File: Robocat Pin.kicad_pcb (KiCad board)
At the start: 2 copper layers, 17 parts, among them SW1 SW_DP3T, U1 NA555P

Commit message: Made PCB, should be good to go now
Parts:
- added G***: LOGO, LOGO, F.Cu at (53.0, 70.6)
- added G***: LOGO, LOGO, F.Cu at (52.9, 52.5)
- added G***: LOGO, LOGO, F.Cu at (52.8, 46.6)
- BT1, C1, C2, C3, C4, C5, C6, R1, R2, R3, R4, R5, R6, SW1: moved to B.Cu
- D1, D2: footprint LED_SMD:LED_1206_3216Metric -> Custom Library:1.3x3.2mm LED; moved to B.Cu
- U1: footprint Package_DIP:DIP-8_W7.62mm -> Custom Library:LM555CM; moved to B.Cu
- moved C4 133.8 mm to (31.8, 48.9), turned to 180 degrees
- moved SW1 128.0 mm to (35.6, 73.0), turned to 135 degrees
- moved D1 126.0 mm to (47.6, 47.6), turned to 180 degrees
- moved U1 105.2 mm to (52.7, 26.0), turned to 180 degrees
- moved C2 103.5 mm to (51.4, 69.8), turned to 180 degrees
- moved C5 101.4 mm to (31.1, 57.1), turned to 180 degrees
- moved D2 100.0 mm to (57.8, 47.6), turned to 180 degrees
- moved R4 99.3 mm to (45.1, 78.7), turned to 180 degrees
- moved BT1 85.2 mm to (52.7, 52.7), turned to 180 degrees
- moved C6 82.8 mm to (74.9, 54.0), turned to 180 degrees
- moved R5 79.8 mm to (47.6, 78.7), turned to 180 degrees
- moved R6 79.7 mm to (50.2, 78.7), turned to 180 degrees
- moved R1 76.5 mm to (55.9, 78.7), turned to 180 degrees
- moved R2 76.1 mm to (58.7, 78.7), turned to 180 degrees
- moved R3 76.0 mm to (61.2, 78.7), turned to 180 degrees
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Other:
- board outline added: 62.9 x 62.9 mm

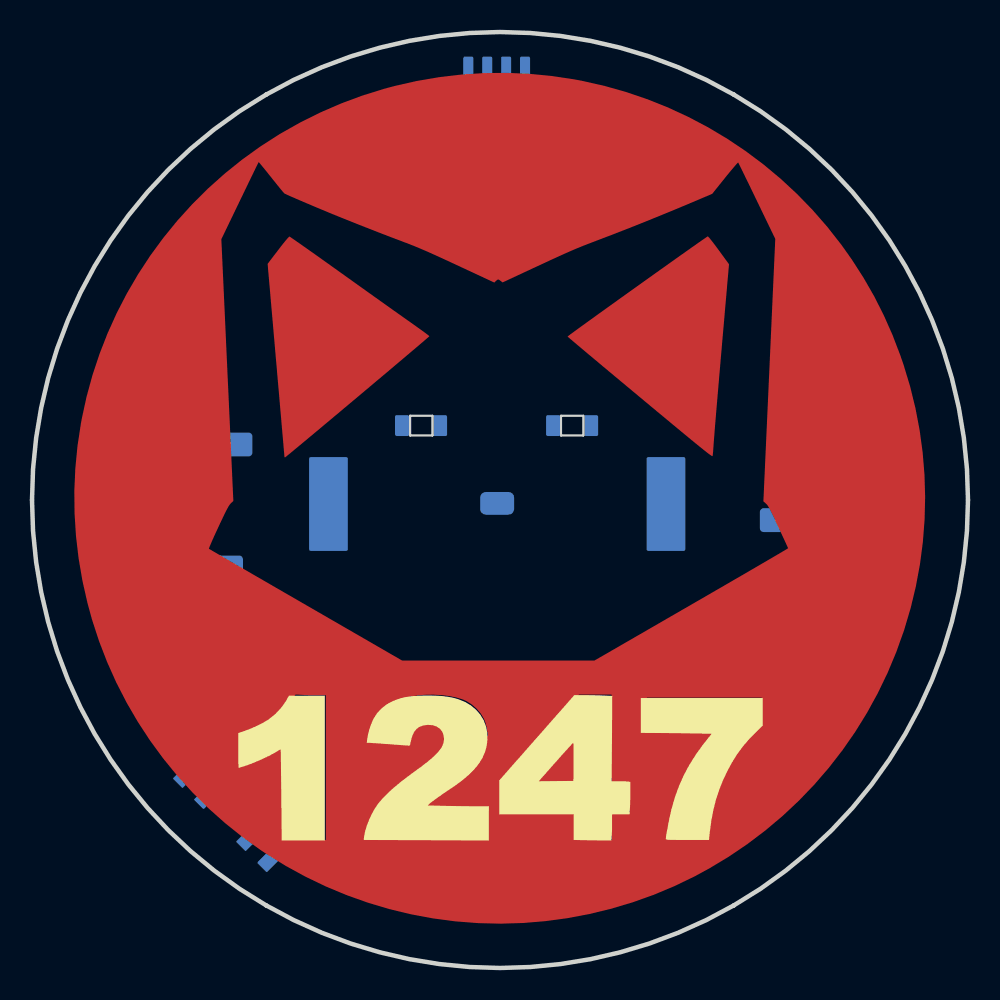
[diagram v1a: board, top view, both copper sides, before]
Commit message: Fixed footprints...need to fix pcb layout (batttery/leds), need to do pcb track
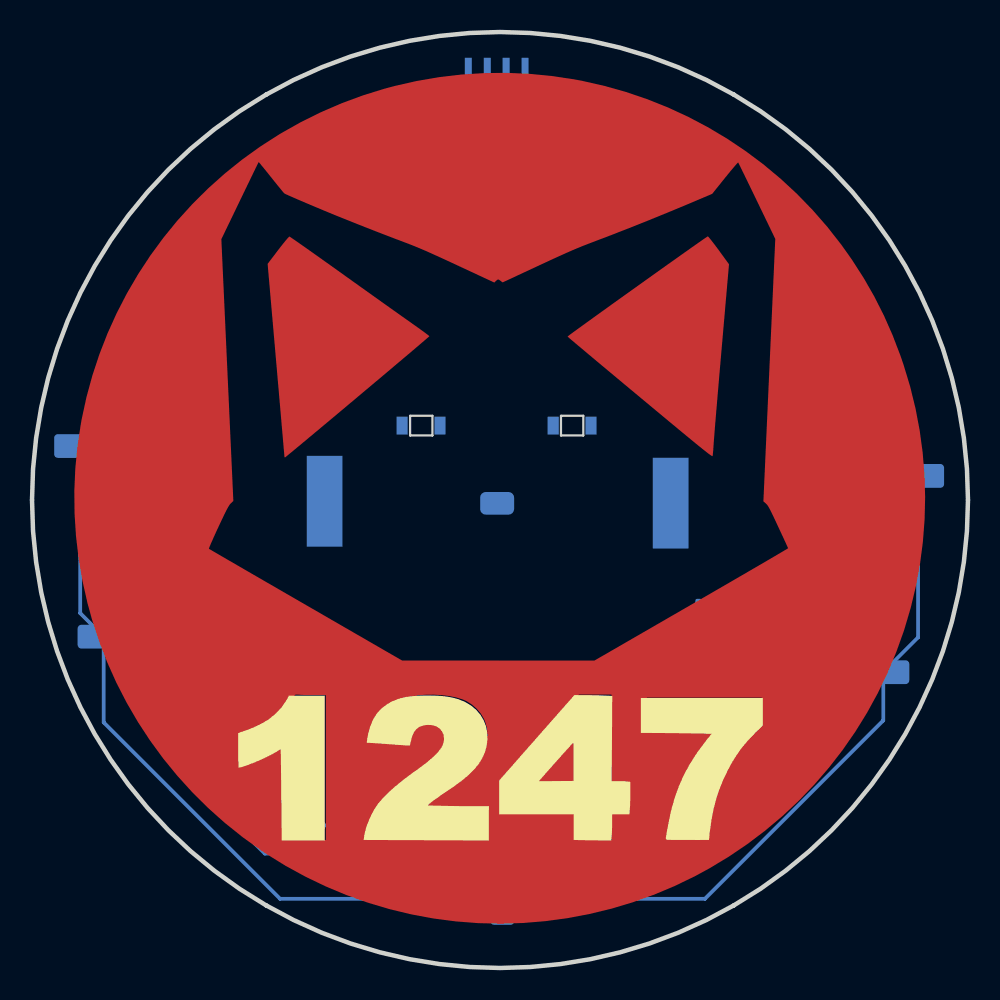
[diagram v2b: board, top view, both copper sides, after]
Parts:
- moved R3 27.0 mm to (37.1, 66.7), turned to 0 degrees
- moved R6 25.3 mm to (66.6, 59.5)
- moved R2 21.6 mm to (39.6, 68.5), turned to 0 degrees
- moved R5 17.9 mm to (63.2, 69.9)
- moved C1 16.7 mm to (62.2, 64.9)
- moved R1 14.5 mm to (45.4, 68.7), turned to 90 degrees
- moved R4 9.11 mm to (41.9, 70.2), turned to 90 degrees
- moved C2 6.96 mm to (53.1, 76.6), turned to 90 degrees
- moved C5 5.06 mm to (29.1, 61.8), turned to 0 degrees
- moved C6 4.42 mm to (78.2, 51.0)
- moved C4 4.22 mm to (27.5, 49.0), turned to 0 degrees
- moved C3 3.72 mm to (75.9, 64.2)
- moved SW1 1.36 mm to (36.9, 72.8)
- turned U1 to 0 degrees
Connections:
- C1 pad 1: Net-(BT1-Pad2) -> Net-(BT1-Pad1)
- C2 pad 2: Net-(BT1-Pad2) -> Net-(BT1-Pad1)
- C3 pad 2: Net-(BT1-Pad2) -> Net-(BT1-Pad1)
- C4 pad 2: Net-(BT1-Pad2) -> Net-(BT1-Pad1)
- C5 pad 2: Net-(BT1-Pad2) -> Net-(BT1-Pad1)
- C6 pad 2: Net-(BT1-Pad2) -> Net-(BT1-Pad1)
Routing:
- net Net-(C2-Pad1): track 0.00 -> 99.3 mm
- net Net-(BT1-Pad1): track 0.00 -> 57.1 mm
- net Net-(R1-Pad1): track 0.00 -> 8.90 mm

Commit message: Rearranged pcb
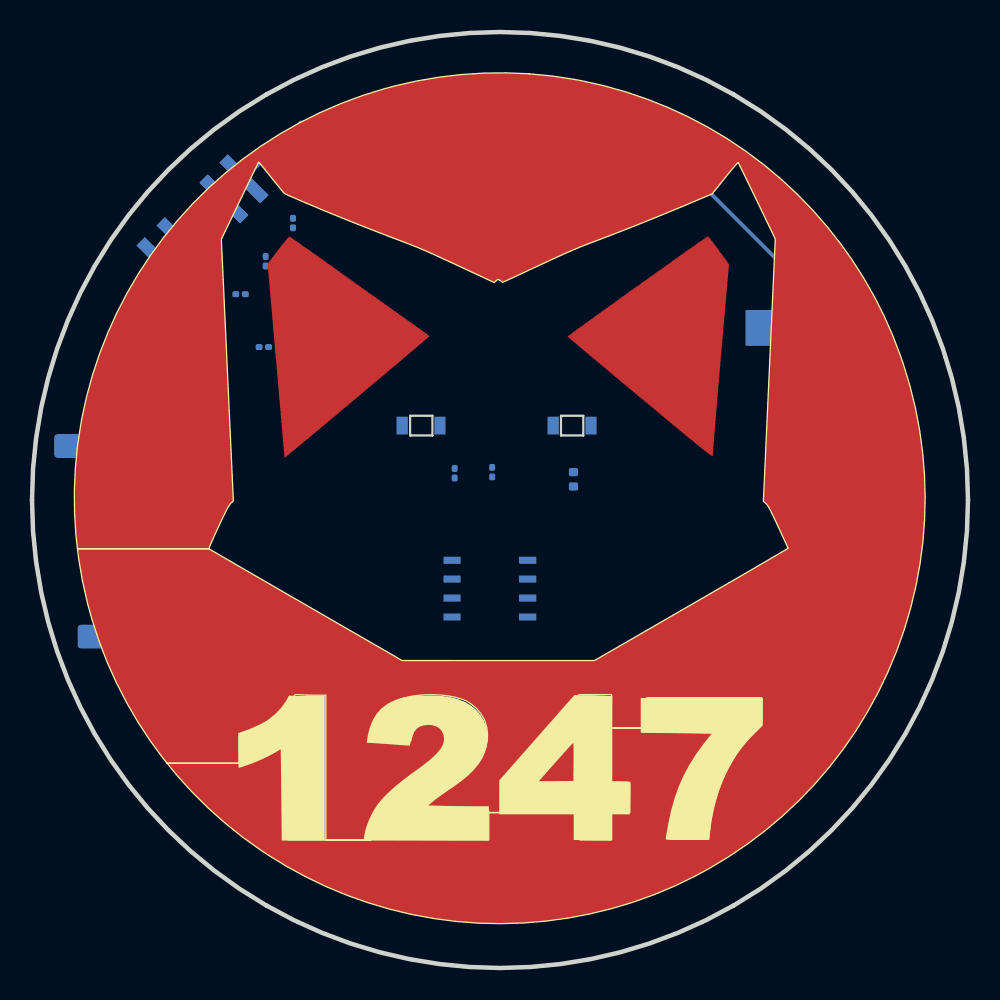
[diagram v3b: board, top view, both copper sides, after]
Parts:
- moved SW1 39.1 mm to (32.9, 33.8), turned to 45 degrees
- moved R3 32.7 mm to (39.0, 34.0), turned to -90 degrees
- moved U1 32.5 mm to (52.2, 58.6), turned to 90 degrees
- moved R4 32.1 mm to (35.5, 38.8), turned to 0 degrees
- moved R2 32.0 mm to (37.2, 36.6), turned to -90 degrees
- moved R1 27.6 mm to (37.1, 42.4), turned to 0 degrees
- moved C3 25.3 mm to (53.0, 74.9), turned to 90 degrees
- moved C6 23.4 mm to (66.4, 71.2)
- moved R5 23.3 mm to (49.9, 50.8), turned to 90 degrees
- moved BT1 19.6 mm to (72.3, 52.7), turned to -90 degrees
- moved R6 16.7 mm to (52.4, 50.7), turned to 90 degrees
- moved C2 15.1 mm to (38.7, 72.1)
- moved C1 14.3 mm to (57.9, 51.2), turned to -90 degrees
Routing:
- net Net-(C2-Pad1): track 99.3 -> 0.00 mm
- net Net-(BT1-Pad1): track 57.1 -> 0.00 mm
- net Net-(BT1-Pad2): track 0.00 -> 48.5 mm
- net Net-(R1-Pad1): track 8.90 -> 0.00 mm

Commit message: Set all the traces
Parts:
- moved C4 2.77 mm to (30.3, 49.0)
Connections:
- net Net-(BT1-Pad1) renamed /gnd
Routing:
- net /gnd: track 0.00 -> 117.3 mm, vias 0 -> 10
- net Net-(C2-Pad1): track 0.00 -> 110.9 mm, vias 0 -> 8
- net Net-(R1-Pad1): track 0.00 -> 56.5 mm
- net Net-(BT1-Pad2): track 48.5 -> 90.5 mm
- net Net-(R1-Pad2): track 0.00 -> 36.1 mm
- net Net-(R5-Pad1): track 0.00 -> 11.0 mm
- net Net-(C1-Pad2): track 0.00 -> 6.23 mm
- net Net-(D2-Pad2): track 0.00 -> 5.26 mm
- net Net-(D1-Pad2): track 0.00 -> 5.22 mm
- net Net-(R4-Pad1): track 0.00 -> 4.78 mm
- net Net-(R3-Pad1): track 0.00 -> 3.25 mm
- net Net-(R2-Pad1): track 0.00 -> 2.71 mm
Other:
- copper layers 2 -> 4

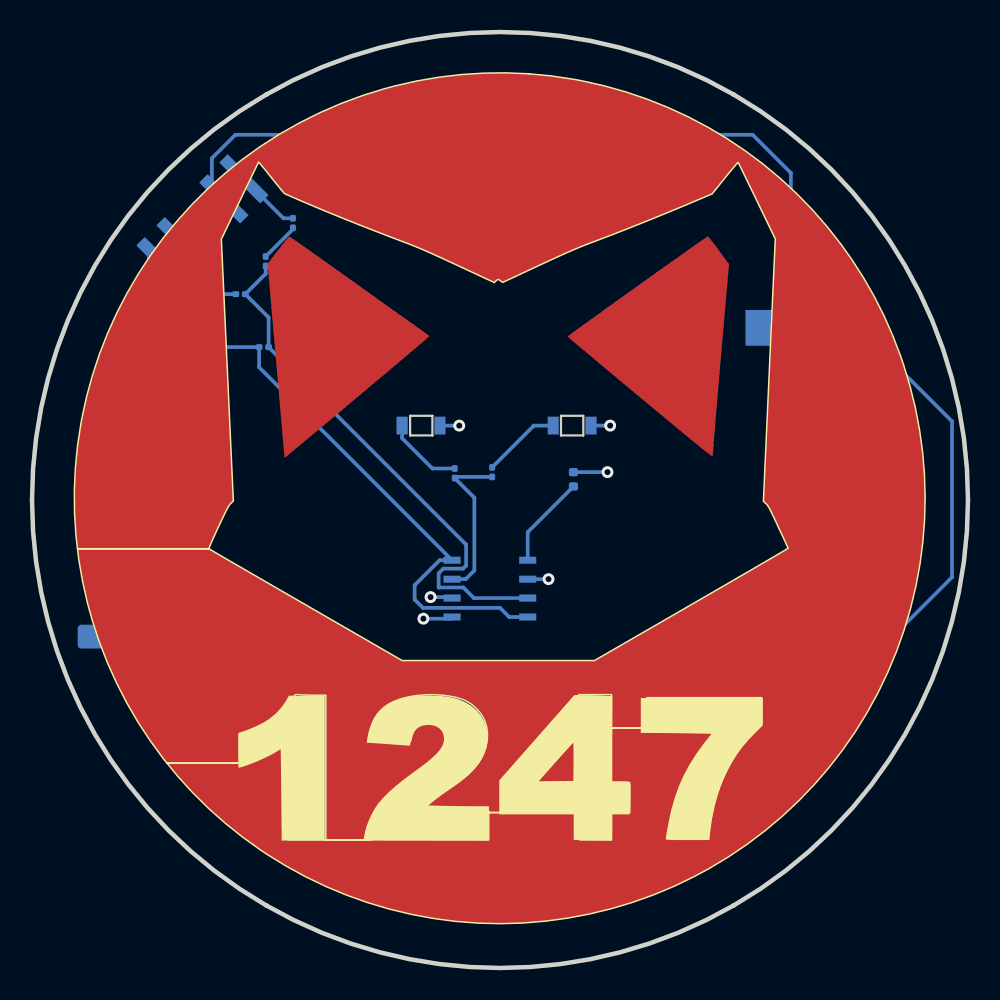
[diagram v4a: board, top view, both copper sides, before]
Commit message: Fixed robocat background
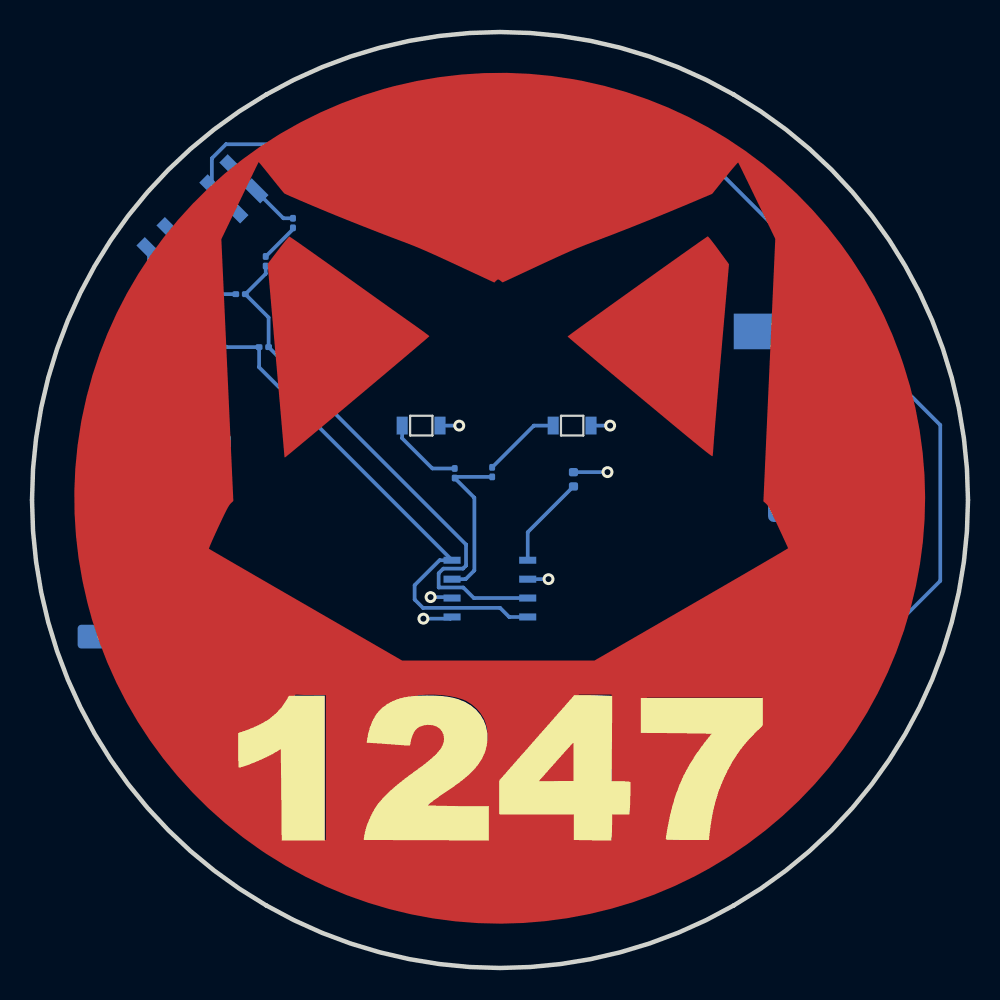
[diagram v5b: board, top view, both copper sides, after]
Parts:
- G***: value LOGO -> Number; footprint LOGO -> Robocat:Number
- G***: value LOGO -> Background; footprint LOGO -> Robocat:Background
- G***: value LOGO -> Face; footprint LOGO -> Robocat:Face
- moved BT1 0.82 mm to (71.6, 53.0)
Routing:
- net Net-(R1-Pad1): track 56.5 -> 51.6 mm
- net Net-(BT1-Pad2): track 90.5 -> 87.7 mm
- net Net-(C2-Pad1): track 110.9 -> 111.7 mm
- net /gnd: track 117.3 -> 116.7 mm

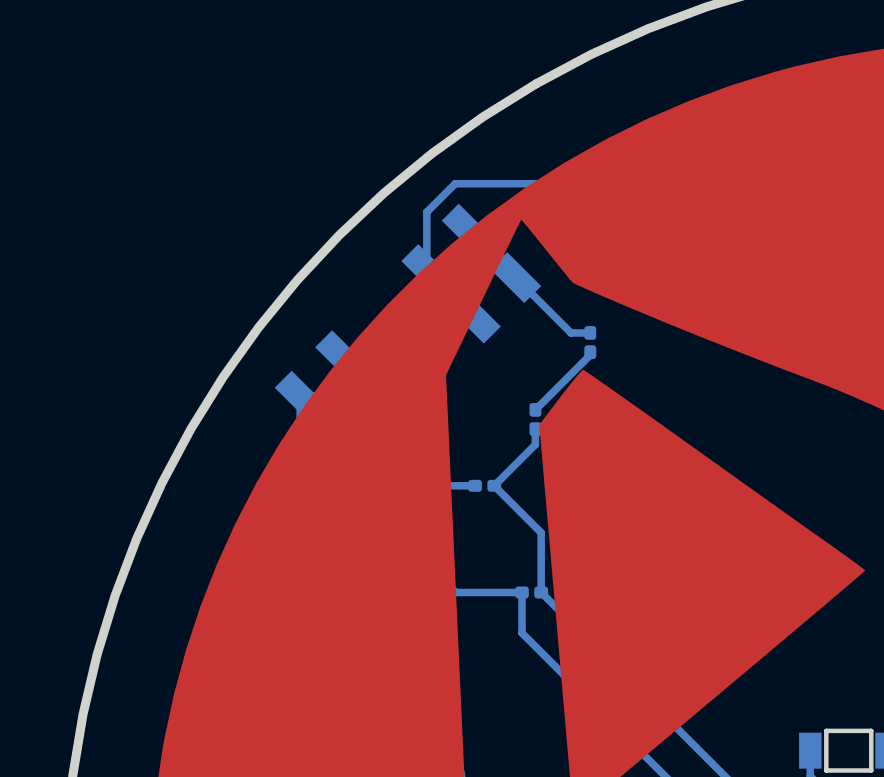
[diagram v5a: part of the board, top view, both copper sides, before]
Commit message: Put 3D models for everything, finished pcb layout
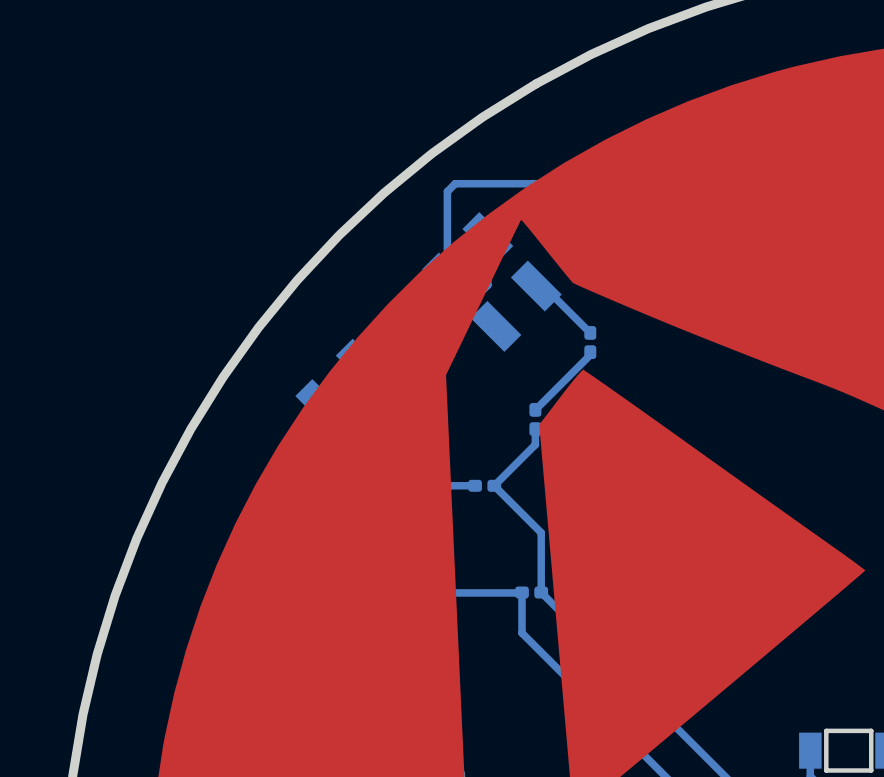
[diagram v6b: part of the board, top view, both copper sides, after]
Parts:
- moved SW1 0.74 mm to (33.6, 34.1)
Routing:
- net Net-(R3-Pad1): track 3.25 -> 2.45 mm
- net Net-(R4-Pad1): track 4.78 -> 3.98 mm
- net Net-(C2-Pad1): track 111.7 -> 112.2 mm
